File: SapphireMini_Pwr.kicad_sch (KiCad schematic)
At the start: 28 parts, among them IC501 SLG59M1446V, J501 JST, Q501 BC857BS, Q502 IRLML6402TRPBF, U501 TPSM84203EAB

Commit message: Start of layout
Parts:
- added D502: MBR230LS, Diode_SMD:D_SOD-123, symbol Diode:MBR0580
- added F501: 1.1A, Resistor_SMD:R_1812_4532Metric, symbol Device:Polyfuse_Small
- C503, C509: footprint Capacitor_SMD:C_0603_1608Metric -> Capacitor_SMD:C_0402_1005Metric
- D501: value MBR180 -> MBR230LS; MPN MBR180S1-7 -> MBR230LS; Manufacturer Diodes Inc -> SMC Diode Solutions
- IC501: MPN (none) -> SLG59M1446V
- Q502: value IRLML6402TRPBF -> SSM3J378R,LXHF; MPN IRLML6402TRPBF -> SSM3J378R,LXHF; Manufacturer Infineon Technologies -> Toshiba Semiconductor and Storage
- R507: MPN (none) -> RMCF0603ZT0R00
- U501: MPN (none) -> TPSM84203EAB
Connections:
- net GND: now also D502.2 (A)
- net at S501.2, S501.6: now also D502.1 (K), F501.2; no longer J501.1 (Pin_1)
- new net: F501.1, J501.1 (Pin_1)
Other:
- note added: "Q502 originallyIRLML6402TRPBF subs FDN302P subs SSM3J378R.LXHF"
- note removed: "Based on TI WEBENCH design for buck 3.4-9V @ 200mA w/ 3.3V output. Efficiency near 90% even at low loads. Choice based on parts availability"
- note removed: "Convert TPS62150 to TPS54332DDAR for parts availability via DigiKey"
- note removed: "Sub FDN302P for IRLML6402TRPBF"
- note removed: "Sub for IRLML6403 Sub for TPS62150 double check design Add connector for vbat_en"

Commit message: updated new layout - no routing
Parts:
- IC501: symbol SamacSys_Parts:SLG59M1446V -> sapphireMini:SLG59M1446V
- S501: symbol JS202011JCQN:JS202011JCQN -> sapphireMini:JS202011JCQN
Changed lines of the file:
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@@
     (pin "2")
   )
-  (symbol (lib_id "JS202011JCQN:JS202011JCQN") (at 48.26 48.26 270) (unit 1)
+  (symbol (lib_id "sapphireMini:JS202011JCQN") (at 48.26 48.26 270) (unit 1)
     (in_bom yes) (on_board yes)
     (property "Reference" "S501" (id 0) (at 54.102 47.0916 90)
@@
     (pin "2")
   )
-  (symbol (lib_id "SamacSys_Parts:SLG59M1446V") (at 62.23 154.94 0) (unit 1)
+  (symbol (lib_id "sapphireMini:SLG59M1446V") (at 62.23 154.94 0) (unit 1)
     (in_bom yes) (on_board yes) (fields_autoplaced)
     (property "Reference" "IC501" (id 0) (at 74.93 148.751 0))

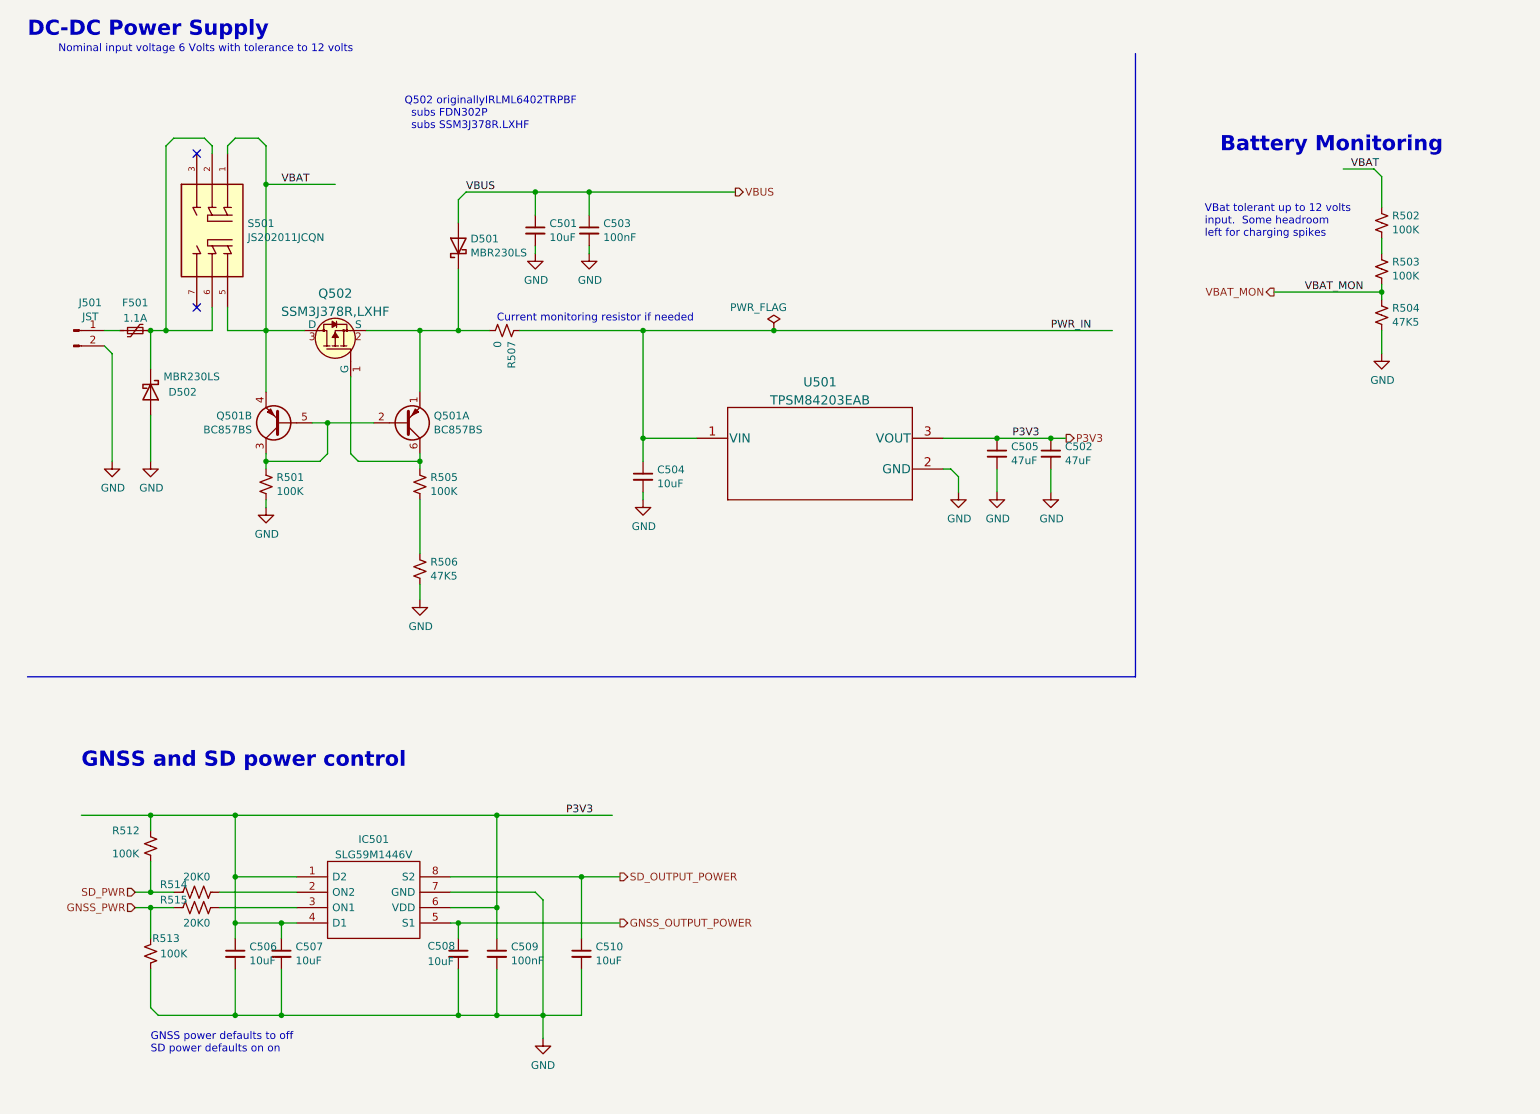
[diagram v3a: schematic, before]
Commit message: 6 Layer Routing
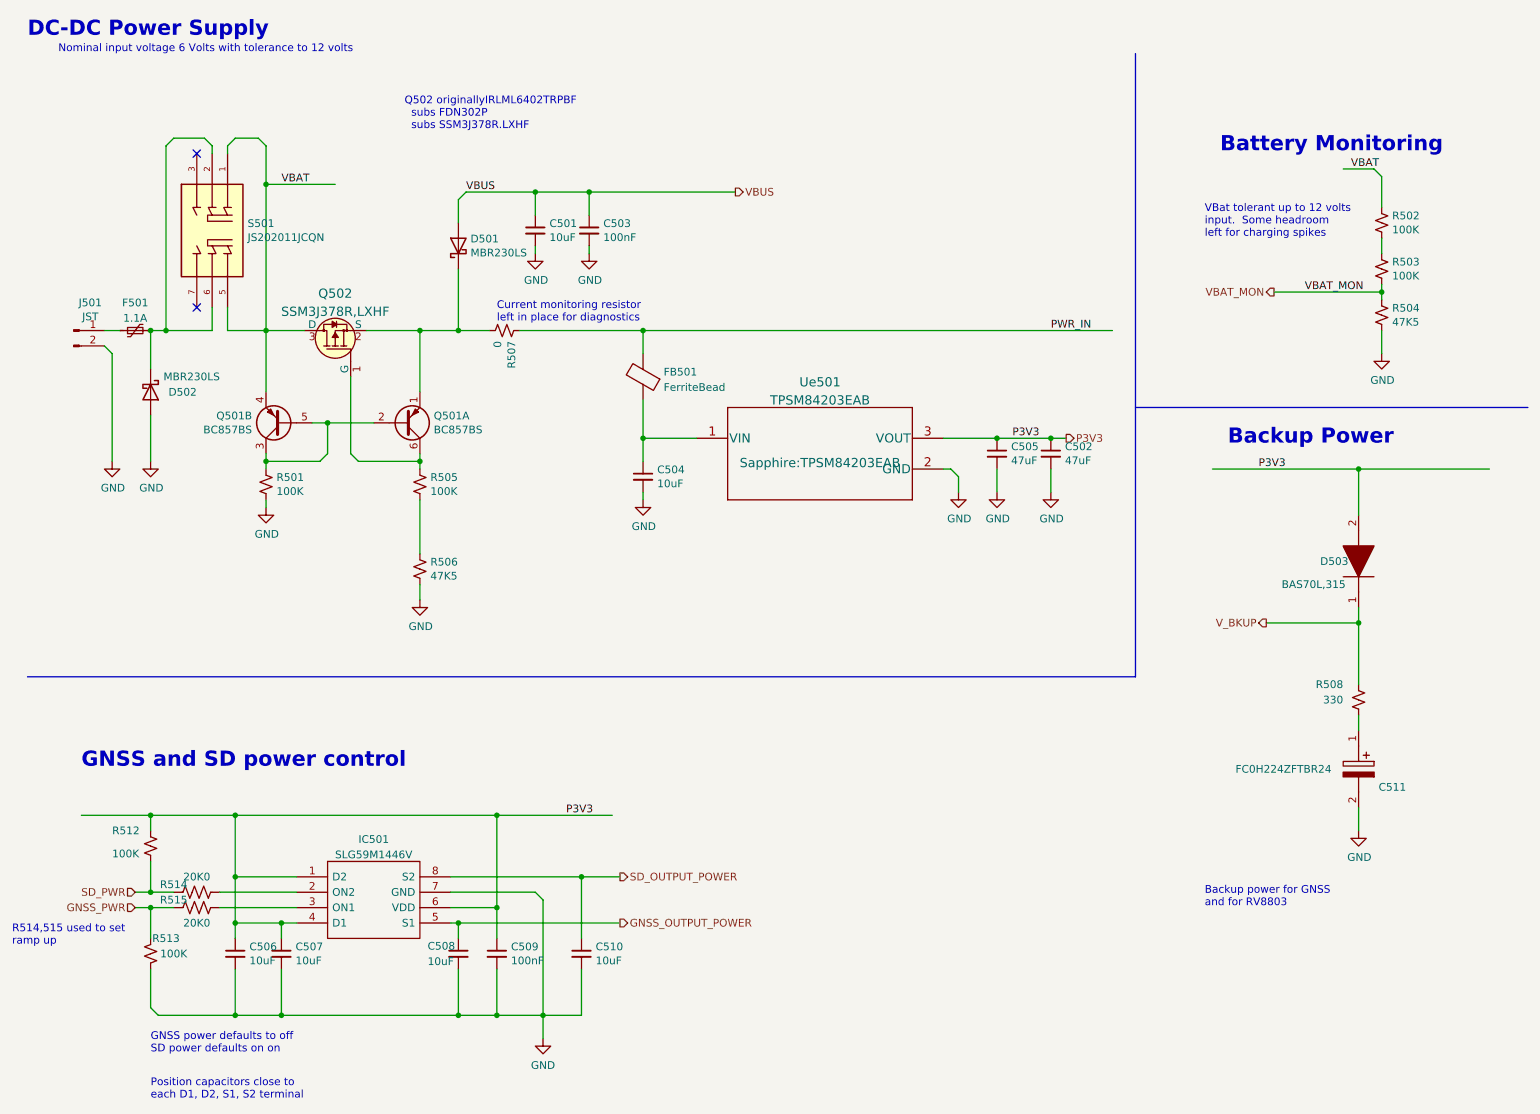
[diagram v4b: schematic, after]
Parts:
- added C511: FC0H224ZFTBR24, CAPAE1080X880N, symbol sapphireMini:FC0H224ZFTBR24
- added D503: BAS70L,315, PESD5V0S1BL315, symbol sapphireMini:BAS70L,315
- added FB501: FerriteBead, Inductor_SMD:L_0603_1608Metric, symbol Device:FerriteBead
- added R508: 330, Resistor_SMD:R_0603_1608Metric, symbol Device:R_Small_US
- J501: footprint Connector_JST:JST_PH_S2B-PH-SM4-TB_1x02-1MP_P2.00mm_Horizontal -> Sapphire:JST_PH_S2B-PH-SM4-TB_1x02-1MP_P2.00mm_Horizontal
- S501: footprint SapphineMinimal:SW_JS202011JCQN -> Sapphire:SW_JS202011JCQN
- renumbered U501 to Ue501
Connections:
- net GND: now also C511.2
- net P3V3: now also D503.2
- net PWR_IN: now also FB501.2; no longer C504.1, Ue501.1 (VIN)
- new net: C511.1, R508.1
- new net: C504.1, FB501.1, Ue501.1 (VIN)
- new net V_BKUP: D503.1, R508.2
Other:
- note added: "Backup Power"
- note added: "Backup power for GNSS and for RV8803"
- note added: "Current monitoring resistor left in place for diagnostics"
- note added: "Position capacitors close to each D1, D2, S1, S2 terminal"
- note added: "R514,515 used to set ramp up"
- note removed: "Current monitoring resistor if needed"

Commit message: Fixing board problems
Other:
- note added: "Use RSCSK2043R3D01007T for C511 as an altrenative. Will require an additional footprint"
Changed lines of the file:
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@@
     (effects (font (size 2.5 2.5) (thickness 0.5) bold) (justify left bottom))
   )
-  (text "Backup power for GNSS\nand for RV8803" (at 212.09 160.02 0)
+  (text "Use RSCSK2043R3D01007T for C511 as\nan altrenative.  Will require an \nadditional footprint"
+    (at 195.58 135.89 0)
     (effects (font (size 1.27 1.27)) (justify left bottom))
   )
+  (text "Backup power for GNSS\nand for RV8803" (at 209.55 143.51 0)
+    (effects (font (size 1.27 1.27)) (justify left bottom))
+  )

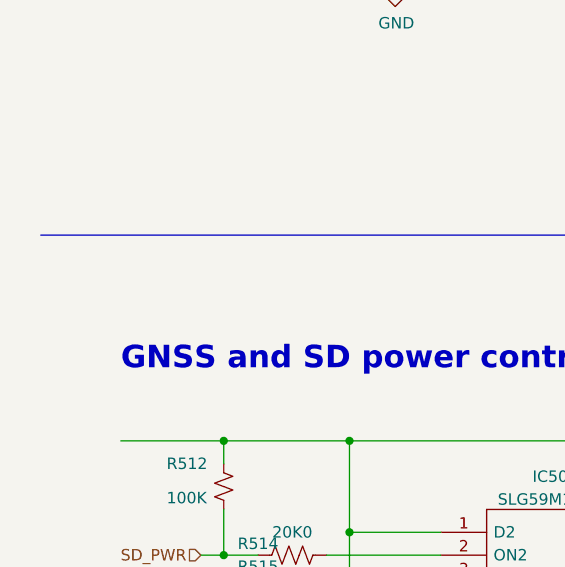
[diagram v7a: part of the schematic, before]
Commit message: Updated PCB comments
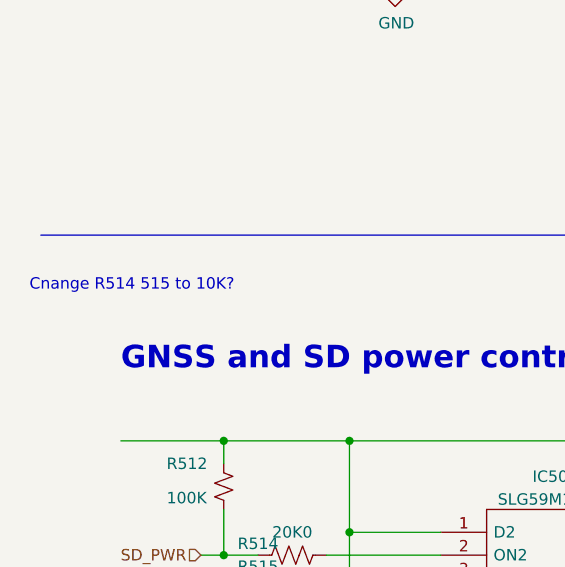
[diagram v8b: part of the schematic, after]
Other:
- note added: "Cnange R514 515 to 10K?"
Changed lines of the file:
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@@
+    (effects (font (size 1.27 1.27)) (justify left bottom))
+  )
+  (text "Cnange R514 515 to 10K?" (at 16.51 128.27 0)
     (effects (font (size 1.27 1.27)) (justify left bottom))
   )
